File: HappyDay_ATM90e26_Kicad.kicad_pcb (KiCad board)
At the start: 2 copper layers, 103 x 51.5 mm, 86 parts, among them J1 Conn_01x03, J10 GS3, J11 GS3, J17 GS3, J18 GS3, J2 TRS3.5Female, J3 TRS3.5Female, M1 ATM90E26_ATM90E26, M2 ATM90E26_ATM90E26, U1 RAC03-3.3SGA, U2 dc-dc, U3 Si865, U4 FeatherHuzzah, Y1 Crystal_Small, Y2 Crystal_Small

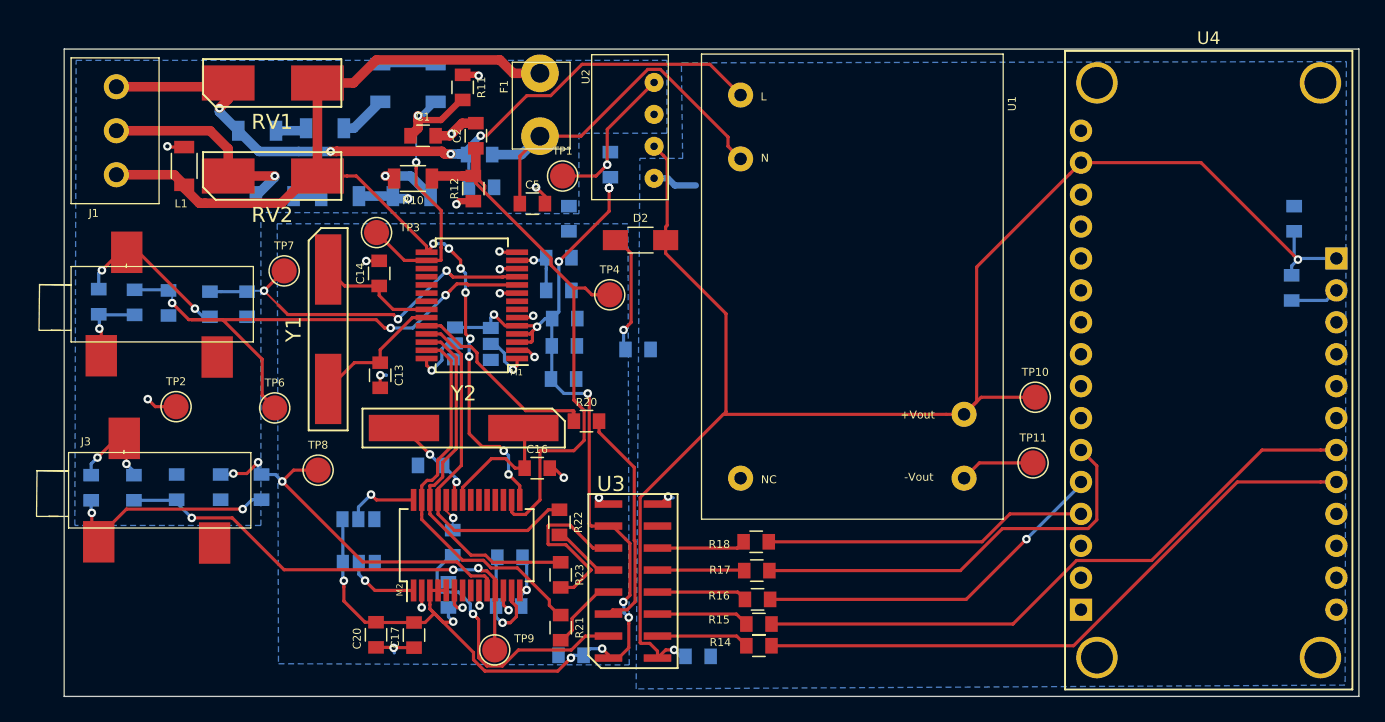
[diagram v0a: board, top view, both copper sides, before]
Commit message: Version b (#1)
* added readme.md to version_B

* added image of PCBs got back from OSHPark

* added image of PCBs got back from OSHPark

* added image of PCBs got back from OSHPark

* added kicad image of voltage sampling

* added voltage sampling test setup image

* added danger electricity image

* updated danger electricity image

* added current sampling kicad image

* added Arduino_AC_current_input_A.png image from OEM site

* added TRS_connector.png

* added scope_current_IP0_andIP1.png

* added test_lamp.jpg

* added RAC03-3.3SGA.png

* added cme0303s3c.png

* modified cme0303S3c.png

* added atm90e26_soldered_on_pcb.jpg

* added atm90e26_schematic.png;

* added Feather_on_PCB.jpg

* add Feather_pins_Schematic.png

* added Schematic_top_sheet.png

* added sense_power_cable.png

* added front_PCB_itemized.png

* added back_PCB_itemized.png

* added Schematic_meter_sheet.png

* added RAC03-caps-from-datasheet.png

* added atm90e26_short_circuit_solder.png

* added PCB_Layout_first_atm90e26_pins.png

* added Logic_analyzer_error.png
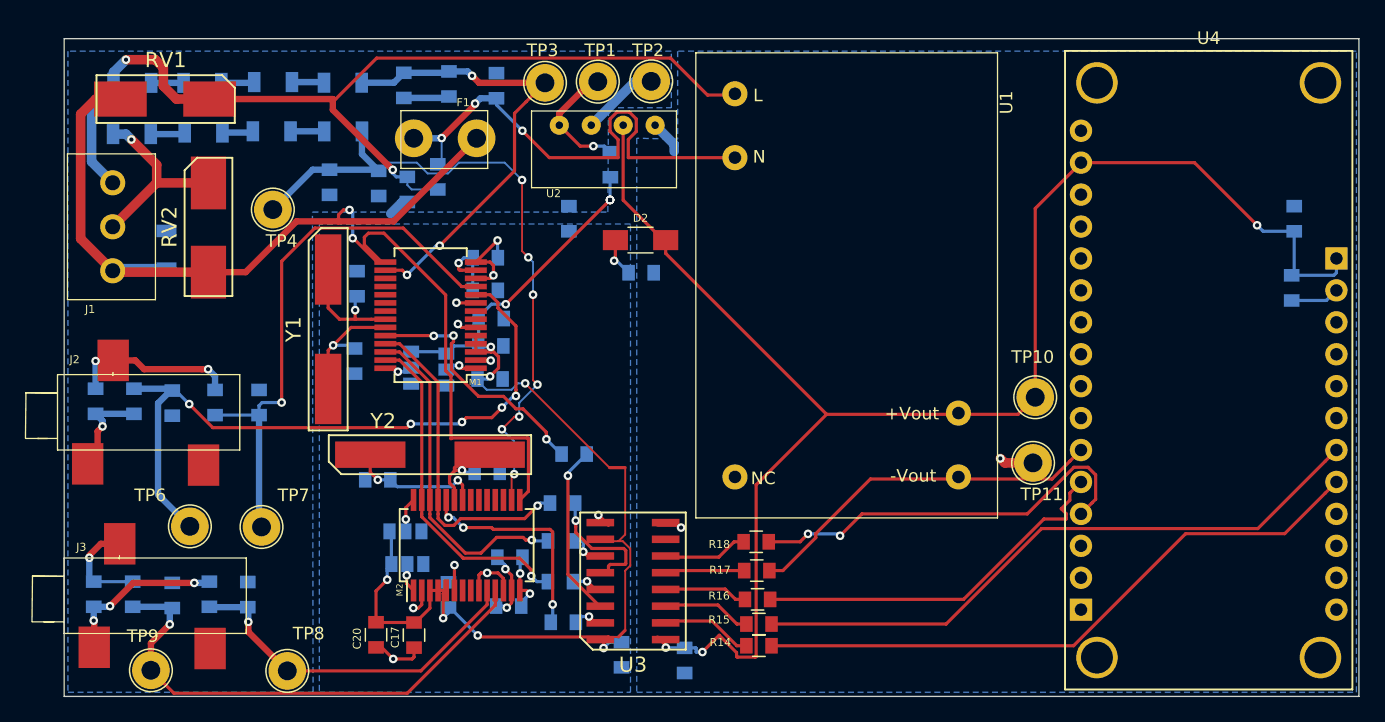
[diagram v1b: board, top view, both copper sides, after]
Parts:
- C1, C13, C14, C16, C2, C5, L1, R10, R11, R12, R20, R21, R22, R23: moved to B.Cu
- TP1, TP10, TP11, TP2, TP3, TP4, TP6, TP7, TP8, TP9: footprint Connectors_TestPoints:Test_Point_Pad_d2.0mm -> Connectors_TestPoints:Test_Point_Loop_D2.54mm_Drill1.5mm_Beaded
- U3: footprint HappyDayEnergyMonitor:Si865 -> HappyDayEnergyMonitor:SOIC-16
- moved TP2 45.8 mm to (117.2, 69.7)
- moved TP4 27.6 mm to (87.2, 79.9)
- moved TP9 27.4 mm to (77.5, 116.5)
- moved TP7 20.4 mm to (86.2, 105.1)
- moved TP3 17.9 mm to (108.8, 69.8)
- moved TP8 16.2 mm to (88.3, 116.6)
- moved C16 12.7 mm to (95.5, 101.4), turned to 180 degrees
- moved R4 12.4 mm to (75.9, 73.9)
- moved R8 12.3 mm to (87.1, 73.6)
- moved R6 12.0 mm to (81.6, 73.8)
- moved TP6 11.6 mm to (80.5, 105.1)
- moved R12 11.5 mm to (91.7, 77.7)
- moved R19 10.8 mm to (110.3, 112.7), turned to 0 degrees
- moved R3 10.6 mm to (76.0, 69.8)
- moved R5 10.4 mm to (81.5, 69.8)
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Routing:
- net Net-(R19-Pad2): track 22.7 -> 2.93 mm
- net L0: track 62.0 -> 77.6 mm, vias 4 -> 3
- net I1N_0: track 29.7 -> 44.8 mm, vias 3 -> 1
- net CS1_ATM: track 2.65 -> 17.5 mm, vias 1 -> 3
- net N: track 82.0 -> 96.7 mm, vias 8 -> 2
- net L0_SAMP: track 26.4 -> 37.2 mm, vias 2 -> 3
- net Net-(R23-Pad2): track 14.3 -> 3.82 mm, vias 0 -> 1
- net I1P_0: track 46.6 -> 55.1 mm, vias 3 -> 5
- net Net-(C4-Pad2): track 32.0 -> 39.8 mm, vias 0 -> 3
- net L1_SAMP: track 46.7 -> 54.0 mm, vias 0 -> 7
- net MISO_MCU: track 25.8 -> 32.4 mm, vias 0 -> 2
- net Net-(D2-Pad1): track 9.65 -> 3.23 mm
- net Net-(R22-Pad2): track 5.06 -> 9.99 mm, vias 0 -> 1
- net Net-(J3-Pad2): track 18.1 -> 13.3 mm, vias 2 -> 3
- net SCLK_MCU: track 33.8 -> 29.0 mm
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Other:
- board size 103 x 51.5 mm -> 103 x 52.3 mm

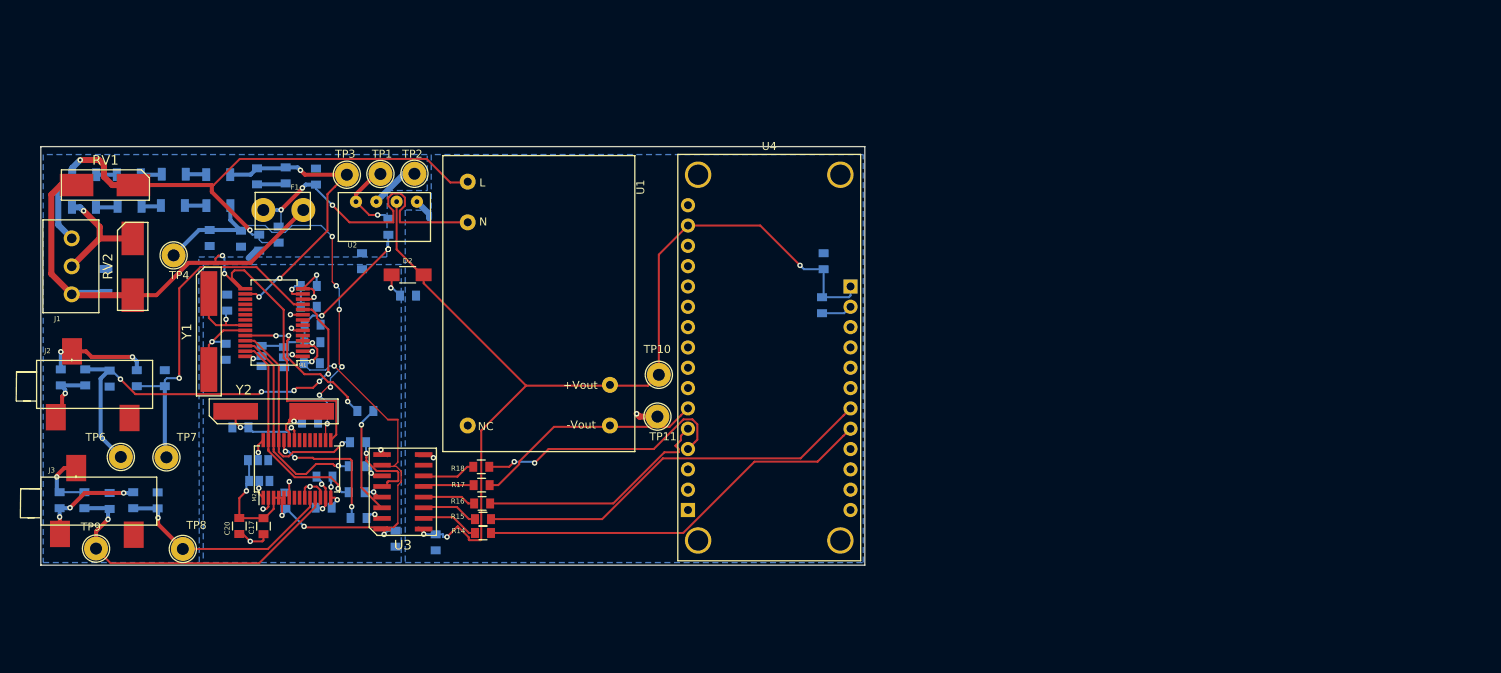
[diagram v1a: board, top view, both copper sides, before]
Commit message: updated design and layout sent to OSH Park (2/26/2018)
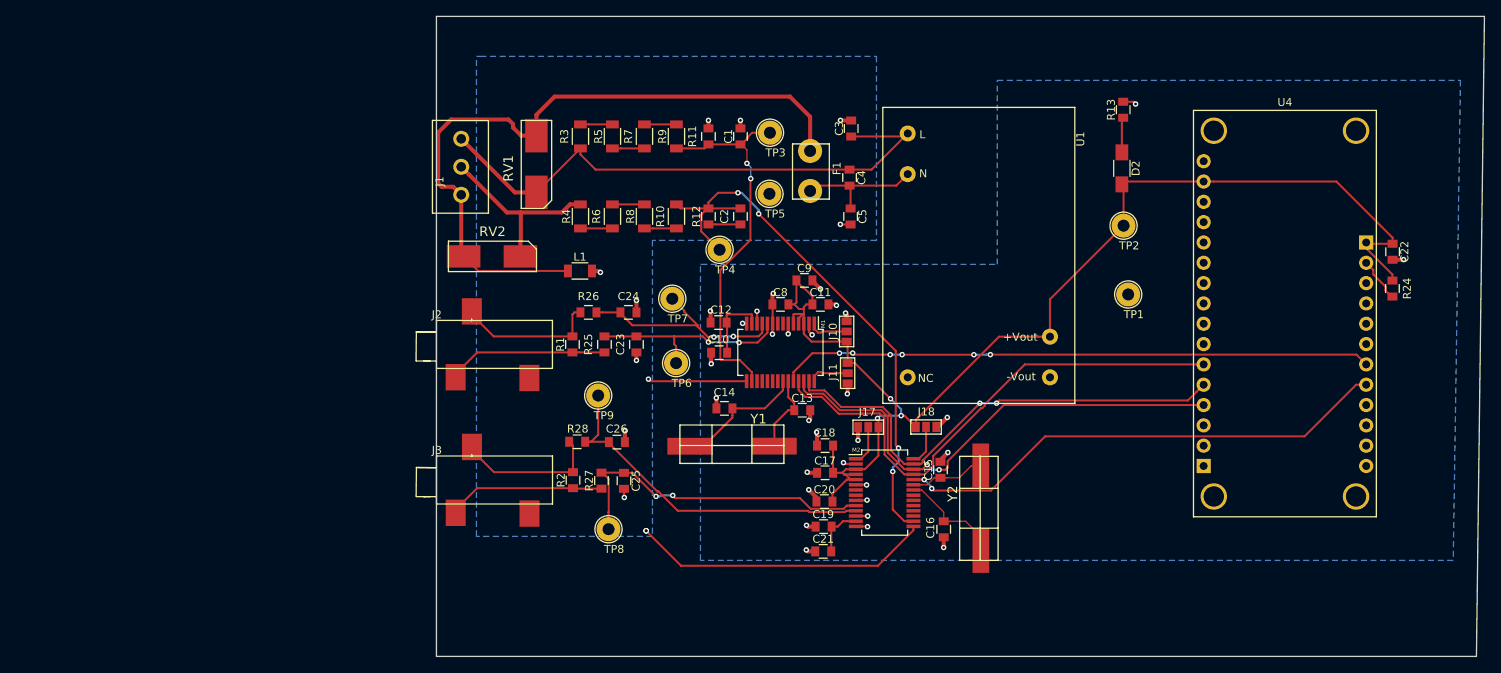
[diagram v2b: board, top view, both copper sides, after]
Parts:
- removed C6, C7: .1u, Capacitors_SMD:C_0805
- removed L2, L3: L_Core_Ferrite_Small, Capacitors_SMD:C_0805
- removed R14, R15, R16, R17, R18, R19, R20, R21, R22, R23: 51, Capacitors_SMD:C_0805
- removed TP10: 3.3V_D, Connectors_TestPoints:Test_Point_Loop_D2.54mm_Drill1.5mm_Beaded
- removed TP11: GND_D, Connectors_TestPoints:Test_Point_Loop_D2.54mm_Drill1.5mm_Beaded
- removed U2: dc-dc, HappyDayEnergyMonitor:DC-DC
- removed U3: Si865, HappyDayEnergyMonitor:SOIC-16
- added TP5: GNDA, Connectors_TestPoints:Test_Point_Loop_D2.54mm_Drill1.5mm_Beaded, F.Cu at (161.6, 72.2)
- C1, C10, C11, C12, C18, C19, C2, C21, C22, C23, C24, C25, C26, C3, C4, C5, C8, C9, J10, J11, J17, J18, L1, R1, R10, R11, R12, R13, R2, R24, R25, R26, R27, R28, R3, R4, R5, R6, R7, R8, R9: moved to F.Cu
- C13, C14, C15, C16: value 27p -> 20p; moved to F.Cu
- J2, J3: value TRS3.5Female -> TRS3.5
- TP1: value 3.3V_A -> GNDD
- TP2: value GNDA -> 3.3V
- TP6: value I1P_0 -> IP_0
- TP7: value I1N_0 -> IN_0
- TP8: value I1P_1 -> IP_1
- TP9: value I1N_1 -> IN_1
- moved TP1 94.7 mm to (206.5, 84.8)
- moved R13 92.4 mm to (205.8, 61.7), turned to 90 degrees
- moved Y2 91.1 mm to (190.2, 109.0), turned to 270 degrees
- moved D2 90.3 mm to (205.7, 69.0), turned to 270 degrees
- moved TP2 88.9 mm to (205.9, 76.2)
- moved C16 88.8 mm to (183.4, 114.1), turned to 270 degrees
- moved J18 83.6 mm to (181.2, 101.3), turned to 90 degrees
- moved C15 79.0 mm to (183.0, 106.7), turned to 90 degrees
- moved J17 76.4 mm to (174.0, 101.3)
- moved C3 75.4 mm to (171.8, 64.0), turned to 90 degrees
- moved M2 73.5 mm to (176.0, 109.5), turned to 0 degrees
- moved J11 73.3 mm to (171.4, 94.6), turned to 0 degrees
- moved C20 73.2 mm to (168.5, 110.7), turned to 180 degrees
- moved C13 72.4 mm to (165.7, 99.2), turned to 0 degrees
- moved C4 71.7 mm to (171.6, 70.2), turned to 270 degrees
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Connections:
- net CLKIN_0 renamed /ATM90_Circuit/CLKIN_0
- net CLKIN_1 renamed /ATM90_Circuit/CLKIN_1
- net CLKOUT_0 renamed /ATM90_Circuit/CLKOUT_0
- net CLKOUT_1 renamed /ATM90_Circuit/CLKOUT_1
- net L0 renamed /LO
- net L0_SAMP renamed /LO_SAMP
- net L1 renamed /L1
- net L1_SAMP renamed /L1_SAMP
- C11 pad 1: +3.3VA -> +3V3
- C17 pad 2: +3.3VA -> +3V3
- C18 pad 1: +3.3VA -> +3V3
- C19 pad 2: Net-(C19-Pad2) -> GNDD
- C2 pad 2: GNDA -> Net-(C2-Pad2)
- C20 pad 1: +3.3VA -> +3V3
- C21 pad 2: Net-(C19-Pad2) -> GNDD
- C22 pad 1: 3.3V_MCU -> +3V3
- C22 pad 2: GND_MCU -> GNDD
- C23 pad 1: I1N_0 -> /IP_0
- C24 pad 2: I1P_0 -> /IN_0
- C25 pad 1: I1N_1 -> /IP_1
- C26 pad 2: I1P_1 -> /IN_1
- C8 pad 2: +3.3VA -> +3V3
- C9 pad 1: +3.3VA -> +3V3
- D2 pad 2: 3.3V_MCU -> +3V3
- F1 pad 2: N -> /N
- J1 pad 3: N -> /N
- J10 pad 3: +3.3VA -> +3V3
- J11 pad 1: +3.3VA -> +3V3
- J17 pad 3: +3.3VA -> +3V3
- J18 pad 1: +3.3VA -> +3V3
- L1 pad 1: N -> /N
- M1 pad 10: I1P_0 -> /IP_0
- M1 pad 11: I1N_0 -> /IN_0
- M1 pad 15: N -> GNDA
- M1 pad 24: CS0_ATM -> /ATM90_Circuit/CS0
- M1 pad 25: SCLK_ATM -> /ATM90_Circuit/SCLK
- M1 pad 26: MISO_ATM -> /ATM90_Circuit/MISO
- M1 pad 27: MOSI_ATM -> /ATM90_Circuit/MOSI
- M1 pad 3: +3.3VA -> +3V3
- M1 pad 4: +3.3VA -> +3V3
- M1 pad 5: +3.3VA -> +3V3
- M2 pad 10: I1P_1 -> /IP_1
- M2 pad 11: I1N_1 -> /IN_1
- M2 pad 14: Net-(C19-Pad2) -> GNDD
- M2 pad 15: N -> GNDA
- M2 pad 24: CS1_ATM -> /ATM90_Circuit/CS1
- M2 pad 25: SCLK_ATM -> /ATM90_Circuit/SCLK
- M2 pad 26: MISO_ATM -> /ATM90_Circuit/MISO
- M2 pad 27: MOSI_ATM -> /ATM90_Circuit/MOSI
- M2 pad 3: +3.3VA -> +3V3
- M2 pad 4: +3.3VA -> +3V3
- M2 pad 5: +3.3VA -> +3V3
- R1 pad 1: Net-(J2-Pad1) -> Net-(J2-Pad2)
- R1 pad 2: Net-(J2-Pad2) -> Net-(J2-Pad1)
- R12 pad 1: GNDA -> Net-(C2-Pad2)
- R13 pad 2: GND_MCU -> GNDD
- R2 pad 1: Net-(J3-Pad1) -> Net-(J3-Pad2)
- R2 pad 2: Net-(J3-Pad2) -> Net-(J3-Pad1)
- R24 pad 2: 3.3V_MCU -> +3V3
- R25 pad 1: I1N_0 -> /IP_0
- R25 pad 2: Net-(J2-Pad1) -> Net-(J2-Pad2)
- R26 pad 1: I1P_0 -> /IN_0
- R26 pad 2: Net-(J2-Pad2) -> Net-(J2-Pad1)
- R27 pad 1: I1N_1 -> /IP_1
- R27 pad 2: Net-(J3-Pad1) -> Net-(J3-Pad2)
- R28 pad 1: I1P_1 -> /IN_1
- R28 pad 2: Net-(J3-Pad2) -> Net-(J3-Pad1)
- RV1 pad 1: N -> /N
- RV2 pad 1: N -> /N
- TP1 pad 1: 3.3V_REG_A -> GNDD
- TP2 pad 1: GNDA -> +3V3
- TP6 pad 1: I1P_0 -> /IP_0
- TP7 pad 1: I1N_0 -> /IN_0
- TP8 pad 1: I1P_1 -> /IP_1
- TP9 pad 1: I1N_1 -> /IN_1
- U1 pad 4: GND_MCU -> GNDD
- U1 pad 5: 3.3V_MCU -> +3V3
- U4 pad 13: GND_MCU -> GNDD
- U4 pad 15: 3.3V_MCU -> +3V3
- U4 pad 17: 3.3V_MCU -> +3V3
- U4 pad 23: CS0_MCU -> /ATM90_Circuit/CS0
- U4 pad 24: CS1_MCU -> /ATM90_Circuit/CS1
- U4 pad 4: MISO_MCU -> /ATM90_Circuit/MISO
- U4 pad 5: MOSI_MCU -> /ATM90_Circuit/MOSI
- U4 pad 6: SCLK_MCU -> /ATM90_Circuit/SCLK
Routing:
- net +3V3: track 0.00 -> 156.5 mm, vias 0 -> 3
- net 3.3V_MCU: track 126.4 -> 0.00 mm, vias 3 -> 0
- net +3.3VA: track 98.2 -> 0.00 mm, vias 11 -> 0
- net N: track 96.7 -> 0.00 mm, vias 2 -> 0
- net /N: track 0.00 -> 88.6 mm
- net /ATM90_Circuit/CS0: track 7.70 -> 74.3 mm, vias 0 -> 6
- net /ATM90_Circuit/SCLK: track 0.00 -> 65.4 mm
- net I1P_0: track 55.1 -> 0.00 mm, vias 5 -> 0
- net /ATM90_Circuit/CS1: track 7.89 -> 62.7 mm, vias 0 -> 2
- net /ATM90_Circuit/MISO: track 7.36 -> 62.1 mm, vias 0 -> 2
- net /ATM90_Circuit/MOSI: track 7.30 -> 61.1 mm, vias 0 -> 2
- net CS0_MCU: track 50.7 -> 0.00 mm
- net CS1_MCU: track 50.3 -> 0.00 mm
- net GNDA: track 11.6 -> 60.7 mm, vias 0 -> 12
- net I1N_0: track 44.8 -> 0.00 mm, vias 1 -> 0
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- removed copper zone on B.Cu, net GND_MCU
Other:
- board size 103 x 52.3 mm -> 131 x 80 mm

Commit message: added datasheets
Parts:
- removed R24: 10K, Capacitors_SMD:C_0805
- moved C15 8.32 mm to (190.4, 102.9)
- moved C13 7.43 mm to (161.9, 105.6)
- moved C14 7.36 mm to (153.0, 105.7), turned to 0 degrees
- moved R13 6.62 mm to (210.3, 66.6), turned to 0 degrees
- moved C16 6.14 mm to (189.5, 113.7)
- moved Y2 4.28 mm to (187.6, 105.6)
- moved Y1 3.24 mm to (159.9, 102.7)
- moved J18 1.14 mm to (180.1, 101.4)
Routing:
- net /ATM90_Circuit/SCLK: track 65.4 -> 74.1 mm
- net Net-(R24-Pad1): track 5.65 -> 0.00 mm
- net /ATM90_Circuit/CLKOUT_1: track 9.40 -> 15.0 mm
- net /ATM90_Circuit/MOSI: track 61.1 -> 63.8 mm, vias 2 -> 0
- net +3V3: track 156.5 -> 153.8 mm, vias 3 -> 5
- net /ATM90_Circuit/CLKIN_0: track 16.5 -> 19.1 mm
- net /ATM90_Circuit/MISO: track 62.1 -> 64.5 mm, vias 2 -> 0
- net /ATM90_Circuit/CLKOUT_0: track 9.90 -> 11.3 mm
- net /ATM90_Circuit/CS1: track 62.7 -> 61.8 mm
- net Net-(D2-Pad1): track 4.39 -> 3.74 mm
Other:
- board size 131 x 80 mm -> 124.4 x 62 mm
